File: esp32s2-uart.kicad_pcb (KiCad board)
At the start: 2 copper layers, 44.2 x 14.7 mm, 38 parts, among them J1 USB_C_Receptacle_USB2.0, J2 Conn_01x06, J3 Conn_02x04_Odd_Even, U1 AMS1117-3.3, U2 ESP32-S2FH4, Y1 Crystal_GND24_Small

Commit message: update
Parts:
- removed the J1 at (131.6, 89.9)
- removed the R5 at (140.6, 91.8)
- removed RN1: 2.2k, Resistor_SMD:R_Array_Concave_4x0402
- added C15: TBD, Capacitor_SMD:C_0402_1005Metric, F.Cu at (133.0, 94.4)
- added C16: TBD, Capacitor_SMD:C_0402_1005Metric, F.Cu at (134.1, 94.4)
- added D1: RED, LED_SMD:LED_0603_1608Metric, F.Cu at (125.7, 92.6)
- added D8: PESD5V0S1BA, Diode_SMD:D_SOD-323, B.Cu at (144.8, 100.9)
- added D9: PESD5V0S1BA, Diode_SMD:D_SOD-323, B.Cu at (144.6, 95.5)
- added J2: USB_C_Receptacle_USB2.0, Connector_USB:USB_C_Receptacle_Palconn_UTC16-G, F.Cu at (121.3, 98.0)
- added R3: 1k, Resistor_SMD:R_0402_1005Metric, B.Cu at (128.6, 94.8)
- added R8: 1k, Resistor_SMD:R_0402_1005Metric, B.Cu at (142.8, 103.6)
- added R9: 1k, Resistor_SMD:R_0402_1005Metric, B.Cu at (142.6, 99.4)
- added SW1: SW_Push, Button_Switch_SMD:SW_SPST_B3U-3000P-B, F.Cu at (140.7, 109.5)
- added U3: ESP32-S2FH4, Package_DFN_QFN:QFN-56-1EP_7x7mm_P0.4mm_EP5.6x5.6mm, F.Cu at (130.2, 99.6)
- C10, C8: value TBD -> 10pf
- C2: value 4.7uf -> 10uf
- C3: value 0.1uf -> 10uf; footprint Capacitor_SMD:C_0402_1005Metric -> Capacitor_SMD:C_0603_1608Metric
- C4: value 10uf -> 0.1uf; footprint Capacitor_SMD:C_0603_1608Metric -> Capacitor_SMD:C_0402_1005Metric
- D2: value ESD9B3.3ST5G -> GREEN; footprint Diode_SMD:D_SOD-923 -> LED_SMD:LED_0603_1608Metric
- D3: value LED -> BLUE
- D4: value PESD3V3L4UF -> PESD5V0S1BA; footprint Package_TO_SOT_SMD:SOT-886 -> Diode_SMD:D_SOD-323
- D5, D6: value LED -> PESD5V0S1BA; footprint LED_SMD:LED_0603_1608Metric -> Diode_SMD:D_SOD-323; moved to B.Cu
- D7: renamed from D1; value ESD9B3.3ST5G -> PESD5V0S1BA; footprint Diode_SMD:D_SOD-923 -> Diode_SMD:D_SOD-323; moved to B.Cu
- J1: renamed from J2; footprint Connector_PinHeader_1.27mm:PinHeader_1x06_P1.27mm_Vertical -> Connector_PinHeader_1.00mm:PinHeader_1x06_P1.00mm_Vertical
- J3: value Conn_02x04_Odd_Even -> Conn_02x05_Counter_Clockwise; footprint Connector_PinHeader_2.54mm:PinHeader_2x04_P2.54mm_Horizontal -> my_footprint:Header_2x5_pin
- R1, R2: moved to B.Cu
- R4: value 10k -> 1k; moved to B.Cu
- R5: renamed from R3; moved to B.Cu
- R6: value 0 -> 10k; moved to F.Cu
- R7: value NC -> 10k; moved to F.Cu
- U2: value ESP32-S2FH4 -> USBLC6-2SC6; footprint Package_DFN_QFN:QFN-56-1EP_7x7mm_P0.4mm_EP5.6x5.6mm -> Package_TO_SOT_SMD:SOT-23-6; moved to B.Cu
- moved R7 36.9 mm to (125.2, 99.6), turned to 270 degrees
- moved R6 26.0 mm to (135.6, 95.8), turned to 180 degrees
- moved U2 25.7 mm to (120.5, 97.4), turned to 180 degrees
- moved R4 25.4 mm to (126.6, 94.8)
- moved D4 24.3 mm to (141.0, 101.0)
- moved D6 23.1 mm to (141.0, 98.0)
- moved J3 20.3 mm to (146.1, 93.0)
- moved R2 20.1 mm to (120.7, 100.7)
- moved D5 19.3 mm to (144.5, 98.2)
- moved D11 19.2 mm to (141.8, 97.4)
- moved D10 19.2 mm to (141.8, 98.8)
- moved R1 19.1 mm to (120.7, 99.8)
- moved R5 19.1 mm to (125.2, 95.3), turned to 90 degrees
- moved C10 19.0 mm to (137.6, 101.4), turned to 180 degrees
- moved J1 17.7 mm to (136.4, 103.8)
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- renumbered D7 to D10, D8 to D11
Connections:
- C10 pad 1: Net-(AE1-Pad1) -> Net-(C10-Pad1)
- C8 pad 1: /LNA_IN -> Net-(C8-Pad1)
- D10 pad 2: /VOUT -> +5V
- D11 pad 2: /VOUT -> +5V
- D2 pad 1: Net-(D2-Pad1) -> GND
- D2 pad 2: GND -> Net-(D2-Pad2)
- D4 pad 1: /UART_RX -> /IO0_TMS
- D5 pad 1: Net-(D5-Pad1) -> /CTS_TDI
- D5 pad 2: /VOUT -> GND
- D6 pad 1: Net-(D6-Pad1) -> /RTS_TDO
- D6 pad 2: /VOUT -> GND
- D7 pad 2: Net-(D1-Pad2) -> /UART_TX
- J3 pad 1: /IO0 -> /IO0_TMS
- J3 pad 2: /UART_TX -> /CTS_TDI
- J3 pad 3: /EN -> /RTS_TDO
- J3 pad 4: /UART_RX -> +3V3
- J3 pad 5: /RTS -> +5V
- J3 pad 6: /CTS -> GND
- J3 pad 7: /VOUT -> GND
- J3 pad 8: GND -> /EN_TCK
- R1 pad 2: Net-(D1-Pad2) -> Net-(R1-Pad2)
- R2 pad 2: Net-(D2-Pad1) -> Net-(R2-Pad2)
- R4 pad 1: +3V3 -> Net-(R4-Pad1)
- R4 pad 2: /DBG_EN -> Net-(D2-Pad2)
- R5 pad 1: Net-(R3-Pad1) -> Net-(R5-Pad1)
- R6 pad 2: /VOUT -> /DBG_EN
- R7 pad 1: +5V -> +3V3
- R7 pad 2: /VOUT -> Net-(R7-Pad2)
- U2 pad 1: +3V3 -> Net-(J2-PadA7)
- U2 pad 2: /LNA_IN -> GND
- U2 pad 3: +3V3 -> Net-(J2-PadA6)
- U2 pad 4: +3V3 -> Net-(R2-Pad2)
- U2 pad 5: /DBG_IO0 -> +5V
- U2 pad 6: Net-(U2-Pad6) -> Net-(R1-Pad2)
- Y1 pad 1: Net-(U2-Pad52) -> Net-(C10-Pad1)
- Y1 pad 3: Net-(U2-Pad53) -> Net-(C8-Pad1)
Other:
- board size 44.2 x 14.7 mm -> 30 x 14 mm

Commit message: update
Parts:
- removed J1: Conn_01x06, Connector_PinHeader_1.00mm:PinHeader_1x06_P1.00mm_Vertical
- added TP1: TestPoint, TestPoint:TestPoint_Pad_D1.0mm, F.Cu at (128.5, 113.9)
- added TP2: TestPoint, TestPoint:TestPoint_Pad_D1.0mm, F.Cu at (128.5, 116.9)
- added TP3: TestPoint, TestPoint:TestPoint_Pad_D1.0mm, F.Cu at (131.5, 113.9)
- added TP4: TestPoint, TestPoint:TestPoint_Pad_D1.0mm, F.Cu at (131.5, 116.9)
- added TP5: TestPoint, TestPoint:TestPoint_Pad_D1.0mm, F.Cu at (134.4, 113.8)
- added TP6: TestPoint, TestPoint:TestPoint_Pad_D1.0mm, F.Cu at (134.6, 116.9)
- moved SW1 6.15 mm to (138.8, 103.7), turned to 180 degrees

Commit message: v1.0
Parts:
- removed D6, D7, D8, D9: PESD5V0S1BA, Diode_SMD:D_SOD-323
- added J1: USB_A, Connector_USB:USB_A_CNCTech_1001-011-01101_Horizontal, F.Cu at (113.5, 98.0)
- D4, D5: value PESD5V0S1BA -> PESD5V0L5UY; footprint Diode_SMD:D_SOD-323 -> Package_TO_SOT_SMD:SOT-363_SC-70-6
- J2: footprint Connector_USB:USB_C_Receptacle_Palconn_UTC16-G -> my_footprint:USB_C_Receptacle; moved to B.Cu
- R3, R4, R5, R8, R9: moved to F.Cu
- SW1: footprint Button_Switch_SMD:SW_SPST_B3U-3000P-B -> my_footprint:button
- TP3: moved to B.Cu
- moved TP2 24.4 mm to (131.3, 92.7)
- moved TP4 21.3 mm to (134.0, 95.8)
- moved TP1 21.2 mm to (129.8, 92.7)
- moved TP6 16.7 mm to (135.3, 100.3)
- moved TP3 13.6 mm to (137.0, 101.4)
- moved TP5 12.3 mm to (135.3, 101.5)
- moved R2 10.5 mm to (130.5, 97.0), turned to 90 degrees
- moved R1 9.42 mm to (129.7, 97.0), turned to 90 degrees
- moved U2 7.04 mm to (127.4, 96.3), turned to 0 degrees
- moved R8 4.33 mm to (141.2, 99.6)
- moved D5 3.48 mm to (142.4, 95.4)
- moved R9 3.23 mm to (141.2, 96.5)
- moved D1 2.60 mm to (128.3, 92.5), turned to 270 degrees
- moved D3 2.60 mm to (125.7, 92.5), turned to 270 degrees
- moved SW1 1.54 mm to (140.1, 102.9)
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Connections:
- D4 pad 1: /IO0_TMS -> GND
- D4 pad 2: GND -> (no net)
- D5 pad 1: /CTS_TDI -> GND
- D5 pad 2: GND -> (no net)
- J2 pad A6: Net-(J2-PadA6) -> /USB_D+
- J2 pad A7: Net-(J2-PadA7) -> /USB_D-
- J2 pad B6: Net-(J2-PadA6) -> /USB_D+
- J2 pad B7: Net-(J2-PadA7) -> /USB_D-
- R1 pad 1: /USB_D- -> Net-(R1-Pad1)
- R2 pad 1: /USB_D+ -> Net-(R2-Pad1)
- U2 pad 1: Net-(J2-PadA7) -> /USB_D-
- U2 pad 3: Net-(J2-PadA6) -> /USB_D+
- U3 pad 25: /USB_D- -> Net-(R1-Pad1)
- U3 pad 26: /USB_D+ -> Net-(R2-Pad1)
- U3 pad 37: /CTS_TDI -> (no net)
- U3 pad 39: /UART_TX -> /EN_TCK
- U3 pad 40: /UART_RX -> /CTS_TDI
- U3 pad 41: /EN_TCK -> /UART_RX
- U3 pad 43: (no net) -> /UART_TX
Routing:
- net +3V3: track 0.00 -> 58.0 mm, vias 0 -> 8
- net +5V: track 0.00 -> 42.9 mm, vias 0 -> 5
- net /UART_RX: track 0.00 -> 23.7 mm, vias 0 -> 2
- net /IO0_TMS: track 0.00 -> 23.6 mm, vias 0 -> 3
- net /CTS_TDI: track 0.00 -> 22.1 mm, vias 0 -> 1
- net /RTS_TDO: track 0.00 -> 21.9 mm, vias 0 -> 1
- net /EN_TCK: track 0.00 -> 21.9 mm, vias 0 -> 1
- net /UART_TX: track 0.00 -> 20.6 mm, vias 0 -> 3
- net /DBG_IO0: track 0.00 -> 20.4 mm, vias 0 -> 4
- net Net-(R2-Pad1): track 0.00 -> 10.2 mm, vias 0 -> 1
- net Net-(R1-Pad1): track 0.00 -> 10.1 mm, vias 0 -> 1
- net GND: track 0.00 -> 8.38 mm, vias 0 -> 47
- net Net-(C10-Pad1): track 0.00 -> 7.19 mm
- net /USB_D+: track 0.00 -> 6.68 mm, vias 0 -> 2
- net /USB_D-: track 0.00 -> 6.04 mm, vias 0 -> 1
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- added copper zone on B.Cu, net GND
- added copper zone on F.Cu, net GND
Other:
- outline, holes or cut-outs redrawn
- net class Default: clearance 0.2 -> 0.14; trace_width 0.25 -> 0.15; via_dia 0.8 -> 0.4; via_drill 0.4 -> 0.2
- net class power added: clearance 0.14, trace_width 0.25, via_dia 0.4, via_drill 0.2
- rule trace_clearance: 0.2 -> 0.14
- rule trace_min: 0.2 -> 0.13
- rule via_min_drill: 0.3 -> 0.2
- board text added: "V1.0"

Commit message: v1.0
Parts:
- added logo1: logo, my_footprint:ESP-USB-Bridge, B.Cu at (129.5, 92.3)
- D10, D11: value LED -> LED_YELLOW
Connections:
- net /EN_TCK renamed /EN
- D10 pad 2: +5V -> +3V3
- D11 pad 2: +5V -> +3V3
- D4 pad 4: +3V3 -> /TCK
- D4 pad 6: +5V -> /TMS
- D5 pad 3: /IO0_TMS -> /IO0
- J3 pad 1: /IO0_TMS -> /IO0
- J3 pad 4: +3V3 -> /TMS
- J3 pad 5: +5V -> +3V3
- J3 pad 7: GND -> /TCK
- U3 pad 37: (no net) -> /TMS
- U3 pad 42: /IO0_TMS -> /TCK
- U3 pad 44: (no net) -> /IO0
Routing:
- net +5V: track 42.9 -> 15.4 mm, vias 5 -> 2
- net /IO0: track 0.00 -> 25.5 mm, vias 0 -> 3
- net /IO0_TMS: track 23.6 -> 0.00 mm, vias 3 -> 0
- net /TMS: track 0.00 -> 20.6 mm, vias 0 -> 2
- net /TCK: track 0.00 -> 17.1 mm, vias 0 -> 1
- net /USB_D+: track 6.68 -> 7.45 mm
- net +3V3: track 58.0 -> 57.3 mm, vias 8 -> 9
- net /UART_TX: track 20.6 -> 21.2 mm
- net GND: vias 47 -> 61

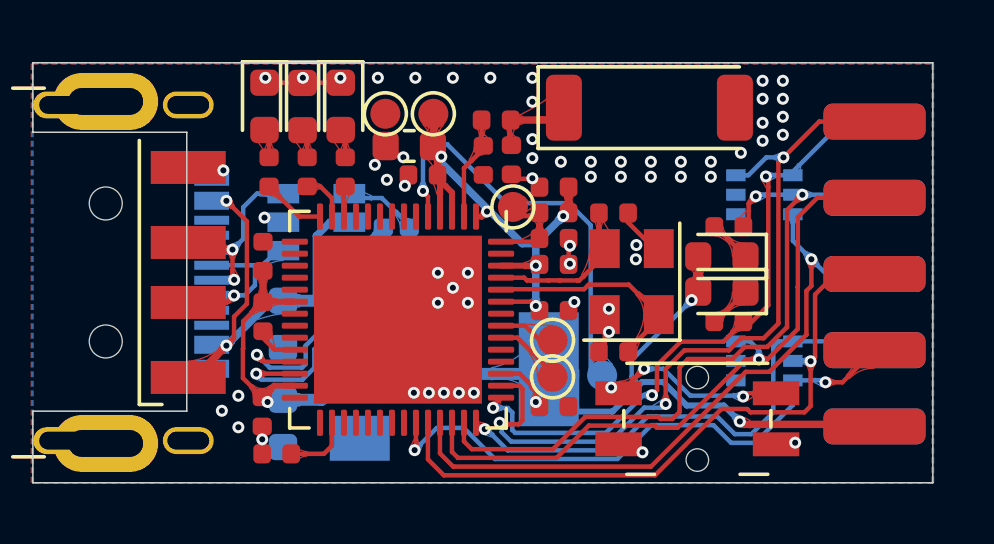
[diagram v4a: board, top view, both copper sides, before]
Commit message: add type-c pull-down resistors
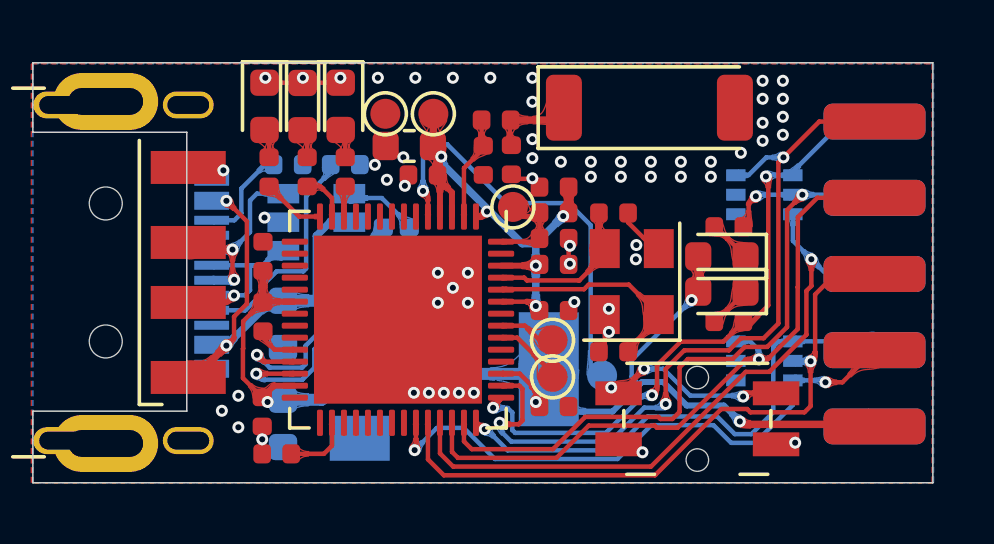
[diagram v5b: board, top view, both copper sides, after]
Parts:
- added R10: 5.1k, Resistor_SMD:R_0402_1005Metric, B.Cu at (128.4, 94.4)
- added R11: 5.1k, Resistor_SMD:R_0402_1005Metric, B.Cu at (126.5, 94.4)
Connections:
- J2 pad A5: (no net) -> Net-(J2-PadA5)
- J2 pad B5: (no net) -> Net-(J2-PadB5)
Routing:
- net Net-(J2-PadA5): track 0.00 -> 7.68 mm
- net Net-(J2-PadB5): track 0.00 -> 3.31 mm

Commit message: v1.0
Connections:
- D4 pad 4: /TCK -> /IO0
- D5 pad 3: /IO0 -> /TCK
- J3 pad 1: /IO0 -> /TCK
- J3 pad 7: /TCK -> /IO0
- U3 pad 42: /TCK -> /IO0
- U3 pad 44: /IO0 -> /TCK
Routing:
- net /TCK: track 17.1 -> 25.5 mm, vias 1 -> 3
- net /IO0: track 25.5 -> 17.1 mm, vias 3 -> 1
